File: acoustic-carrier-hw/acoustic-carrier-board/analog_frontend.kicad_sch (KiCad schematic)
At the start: 33 parts, among them IC1 ECP5-BGA256, J1 8P8C_Shielded, U3 MS9280

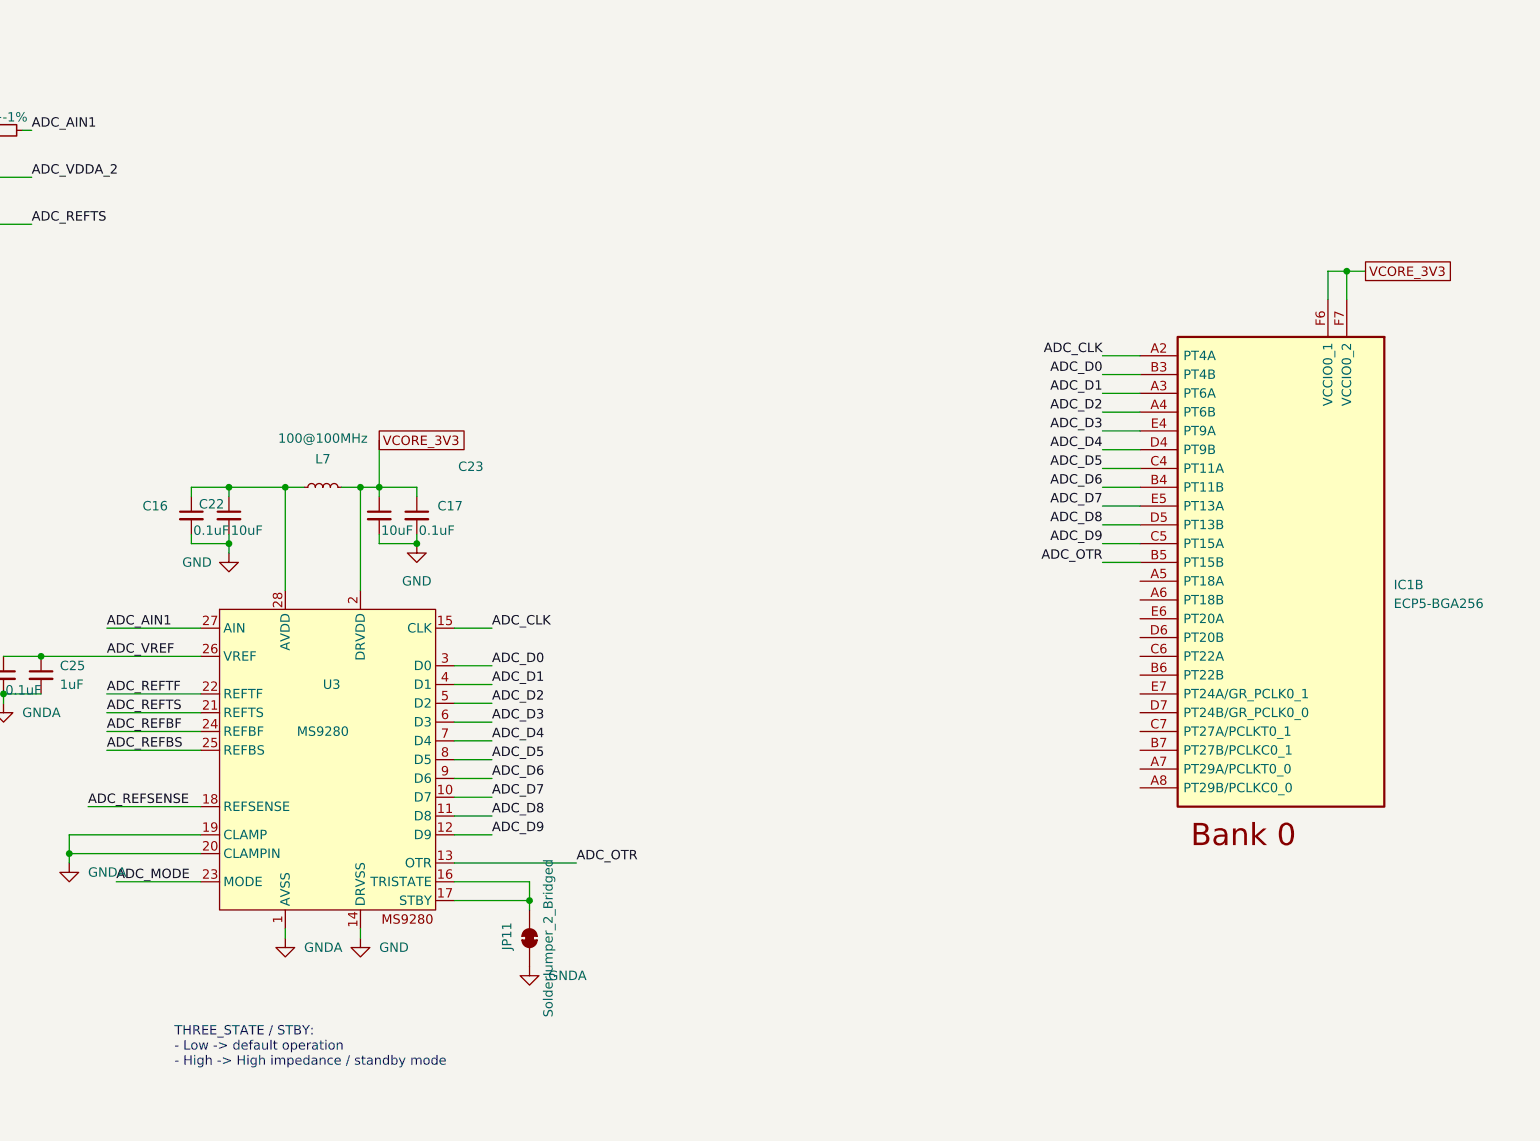
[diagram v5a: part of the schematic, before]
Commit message: [carrier] Added adc connections and PWM + poweer connectors
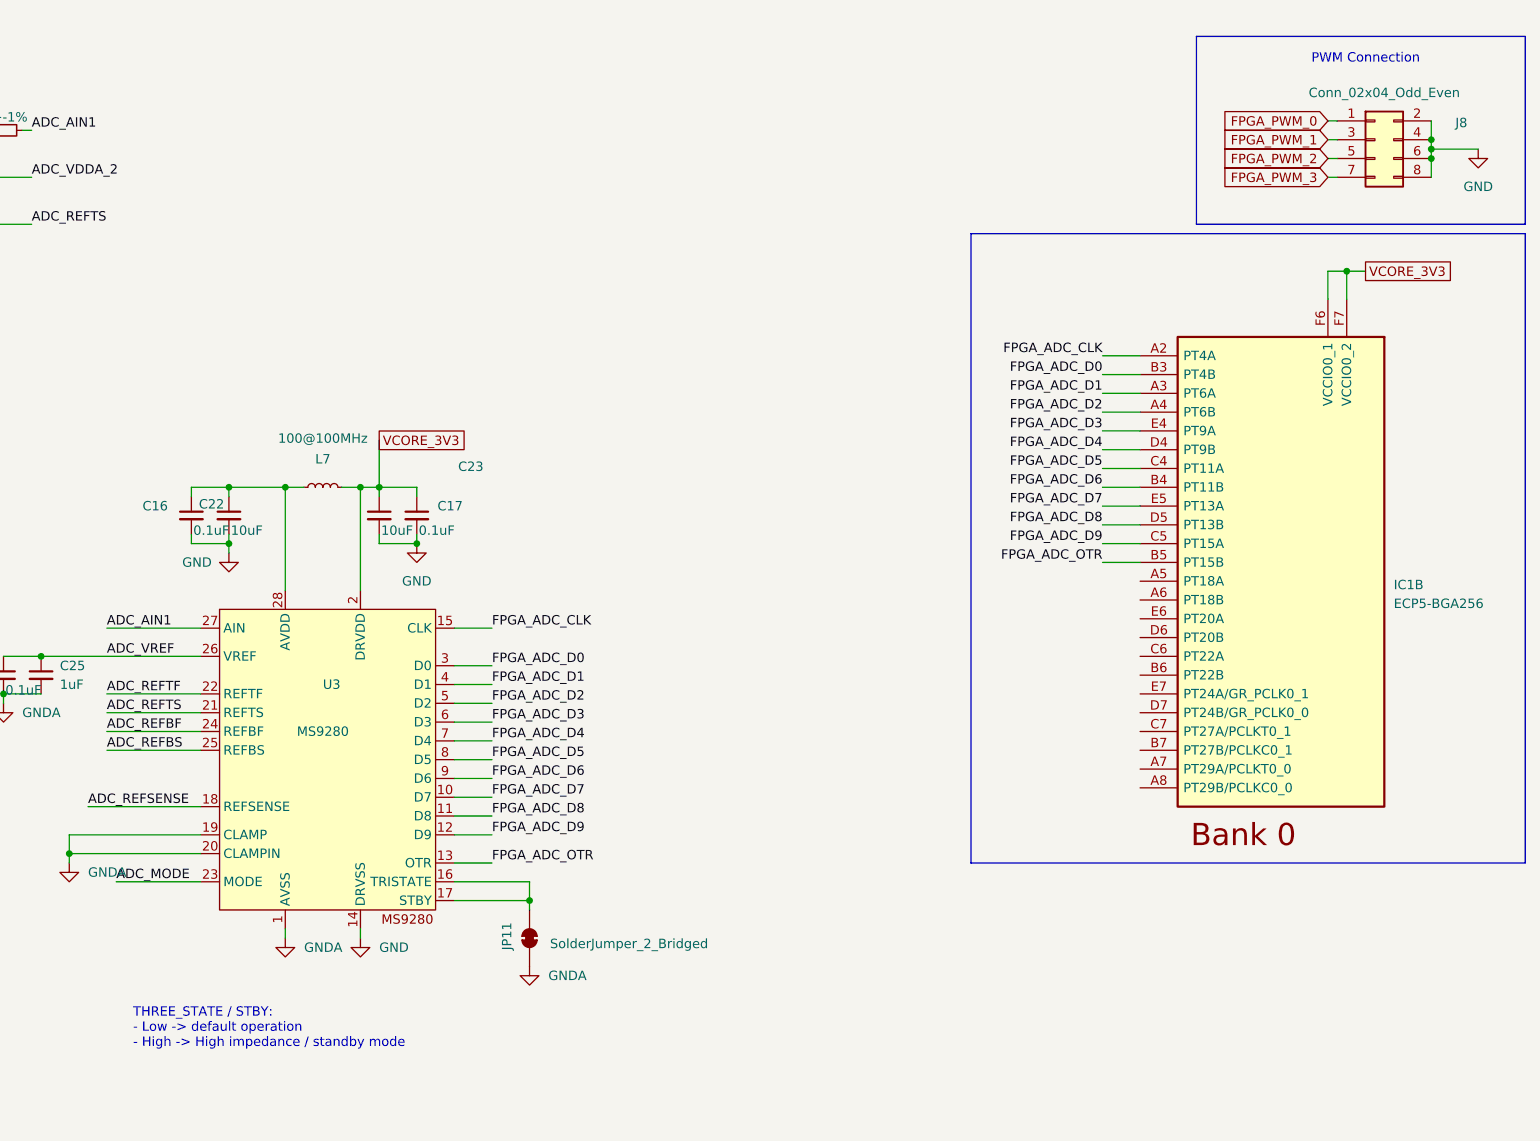
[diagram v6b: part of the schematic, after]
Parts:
- added J8: Conn_02x04_Odd_Even, Connector_PinSocket_2.54mm:PinSocket_2x04_P2.54mm_Horizontal, symbol Connector_Generic:Conn_02x04_Odd_Even
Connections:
- net GND: now also J8.2 (Pin_2), J8.4 (Pin_4), J8.6 (Pin_6), J8.8 (Pin_8)
- net ADC_CLK renamed FPGA_ADC_CLK
- net ADC_D0 renamed FPGA_ADC_D0
- net ADC_D1 renamed FPGA_ADC_D1
- net ADC_D2 renamed FPGA_ADC_D2
- net ADC_D3 renamed FPGA_ADC_D3
- net ADC_D4 renamed FPGA_ADC_D4
- net ADC_D5 renamed FPGA_ADC_D5
- net ADC_D6 renamed FPGA_ADC_D6
- net ADC_D7 renamed FPGA_ADC_D7
- net ADC_D8 renamed FPGA_ADC_D8
- net ADC_D9 renamed FPGA_ADC_D9
- net ADC_OTR renamed FPGA_ADC_OTR
- new net FPGA_PWM_0: J8.1 (Pin_1)
- new net FPGA_PWM_1: J8.3 (Pin_3)
- new net FPGA_PWM_2: J8.5 (Pin_5)
- new net FPGA_PWM_3: J8.7 (Pin_7)
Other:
- note added: "PWM Connection"

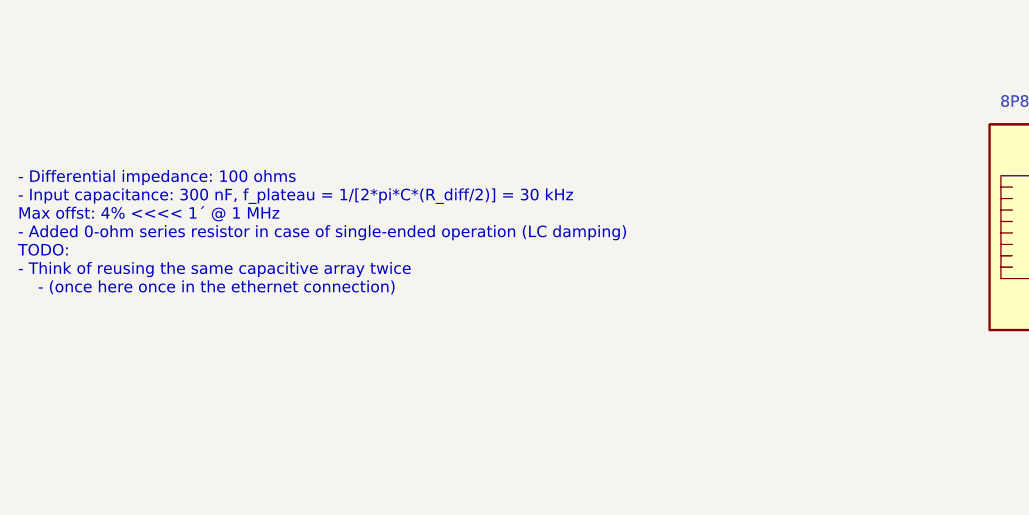
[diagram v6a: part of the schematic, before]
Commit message: [carrier] Reordered carrier board (next) add magnetics to adc differential and ethernet instead of capacitors - SRF is too low
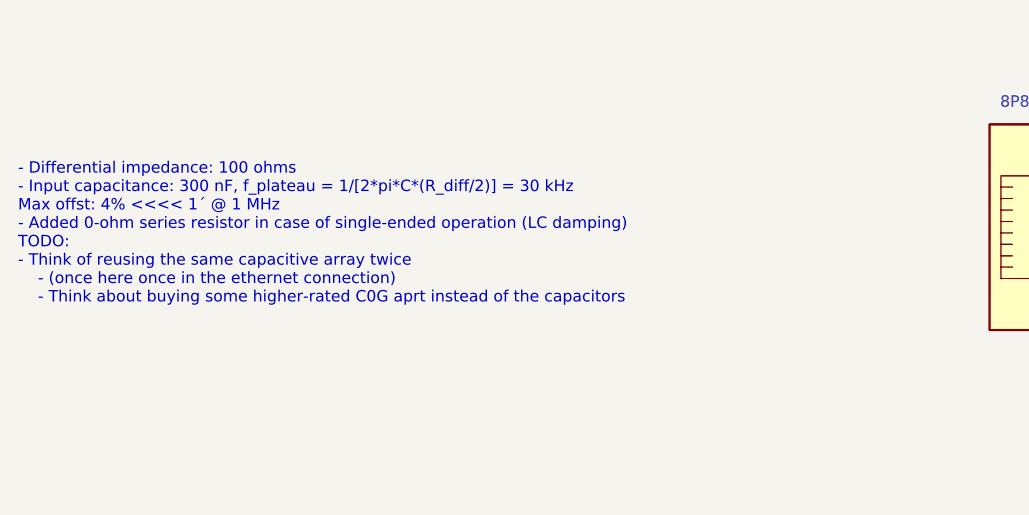
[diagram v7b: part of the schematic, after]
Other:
- note added: "- Differential impedance: 100 ohms - Input capacitance: 300 nF, f_plateau = 1/[2*pi*C*(R_diff/2)] = 30 kHz Max offst: 4% <<<< 1´ @ 1 MHz - Added 0-ohm series resistor in case of single-ended operation (LC damping) TODO: - Think of reusing the same capacitive array twice - (once here once in the ethernet connection) - Think about buying some higher-rated C0G aprt instead of the capacitors"
- note removed: "- Differential impedance: 100 ohms - Input capacitance: 300 nF, f_plateau = 1/[2*pi*C*(R_diff/2)] = 30 kHz Max offst: 4% <<<< 1´ @ 1 MHz - Added 0-ohm series resistor in case of single-ended operation (LC damping) TODO: - Think of reusing the same capacitive array twice - (once here once in the ethernet connection)"
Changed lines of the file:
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@@
 		)
 	)
-	(text "- Differential impedance: 100 ohms\n- Input capacitance: 300 nF, f_plateau = 1/[2*pi*C*(R_diff/2)] = 30 kHz\nMax offst: 4% <<<< 1´ @ 1 MHz\n- Added 0-ohm series resistor in case of single-ended operation (LC damping)\nTODO:\n- Think of reusing the same capacitive array twice \n	- (once here once in the ethernet connection)"
+	(text "- Differential impedance: 100 ohms\n- Input capacitance: 300 nF, f_plateau = 1/[2*pi*C*(R_diff/2)] = 30 kHz\nMax offst: 4% <<<< 1´ @ 1 MHz\n- Added 0-ohm series resistor in case of single-ended operation (LC damping)\nTODO:\n- Think of reusing the same capacitive array twice \n	- (once here once in the ethernet connection)\n	- Think about buying some higher-rated C0G aprt instead of the capacitors"
 		(exclude_from_sim no)
 		(at -87.63 69.342 0)

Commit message: [carrier] Reorganized carrier board schematic, added lcsc part numbers (next) check schematic before component placement
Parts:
- C16, C17, C24, C26, C27, C29: LCSC Part Number C307331 -> (none); LPN (none) -> C307331; MPN (none) -> CL05B104KB54PNC; Manufacturing Part Number CL05B104KB54PNC -> (none)
- C22, C23, C28: LCSC Part Number C19702 -> (none); LPN (none) -> C19702; MPN (none) -> CL10A106KP8NNNC; Manufacturing Part Number CL10A106KP8NNNC -> (none)
- C25: LCSC Part Number C28323 -> (none); LPN (none) -> C28323; MPN (none) -> CL21B105KBFNNNE; Manufacturing Part Number CL21B105KBFNNNE -> (none)
- C30, C31: LCSC Part Number C88136 -> (none); LPN (none) -> C88136; MPN (none) -> 0603B104J500NT; Manufacturing Part Number 0603B104J500NT -> (none)
- J1: LCSC Part Number C708652 -> (none); LPN (none) -> C708652; MPN (none) -> RC01937; Manufacturing Part Number RC01937 -> (none)
- R11, R12, R13, R14: LCSC Part Number C25900 -> (none); LPN (none) -> 0402WGF4701TCE; MPN (none) -> C25900; Manufacturing Part Number 0402WGF4701TCE -> (none)
- R15, R16: LCSC Part Number C23197 -> (none); LPN (none) -> 0603WAF510JT5E; MPN (none) -> C23197; Manufacturing Part Number 0603WAF510JT5E -> (none)
- R17: LCSC Part Number C17477 -> (none); LPN (none) -> 0805W8F0000T5E; MPN (none) -> C17477; Manufacturing Part Number 0805W8F0000T5E -> (none)
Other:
- note added: "- Differential impedance: 100 ohms - Input capacitance: 300 nF, f_plateau = 1/[2*pi*C*(R_diff/2)] = 30 kHz Max offst: 4% <<<< 1´ @ 1 MHz - Added 0-ohm series resistor in case of single-ended operation (LC damping)"
- note added: "ADC FRONTEND"
- note added: "ADC SETTINGS"
- note added: "FPGA BANK"
- note added: "PWM CONNECTOR"
- note added: "TODO: - Think of reusing the same capacitive array twice - (once here once in the ethernet connection) - Think about buying some higher-rated C0G aprt instead of the capacitors - You'll need to add magnetics, c0G capacitors of that side = $$$ - Add extra BOOST/SEPIC-enable signals to connector"
- note removed: "- Differential impedance: 100 ohms - Input capacitance: 300 nF, f_plateau = 1/[2*pi*C*(R_diff/2)] = 30 kHz Max offst: 4% <<<< 1´ @ 1 MHz - Added 0-ohm series resistor in case of single-ended operation (LC damping) TODO: - Think of reusing the same capacitive array twice - (once here once in the ethernet connection) - Think about buying some higher-rated C0G aprt instead of the capacitors"
- note removed: "PWM Connection"
- moved on the sheet: C16, C17, C22, C23, C24, C25, C30, C31, J1, JP11, L7, R15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
